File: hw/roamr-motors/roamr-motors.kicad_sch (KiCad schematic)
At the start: 0 parts

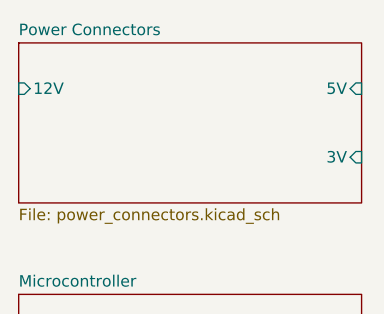
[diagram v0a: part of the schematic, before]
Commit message: Add USB-UART, USB receptacles, ESP32-S3-WROOM-1, switches. TODO: 5V_3V3 LDO, BLDC drivers, encoder SPI, connectors
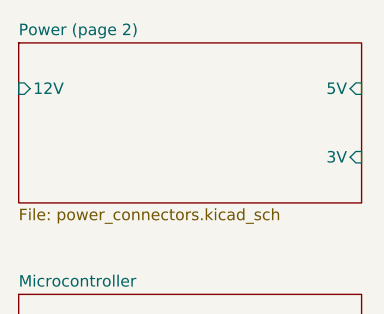
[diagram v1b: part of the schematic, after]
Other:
- sheet Power Connectors renamed Power (page 2)
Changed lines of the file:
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@@
 			(color 0 0 0 0.0000)
 		)
-		(property "Sheetname" "Power Connectors"
+		(property "Sheetname" "Power (page 2)"
 			(at 120.65 43.7384 0)
 			(effects

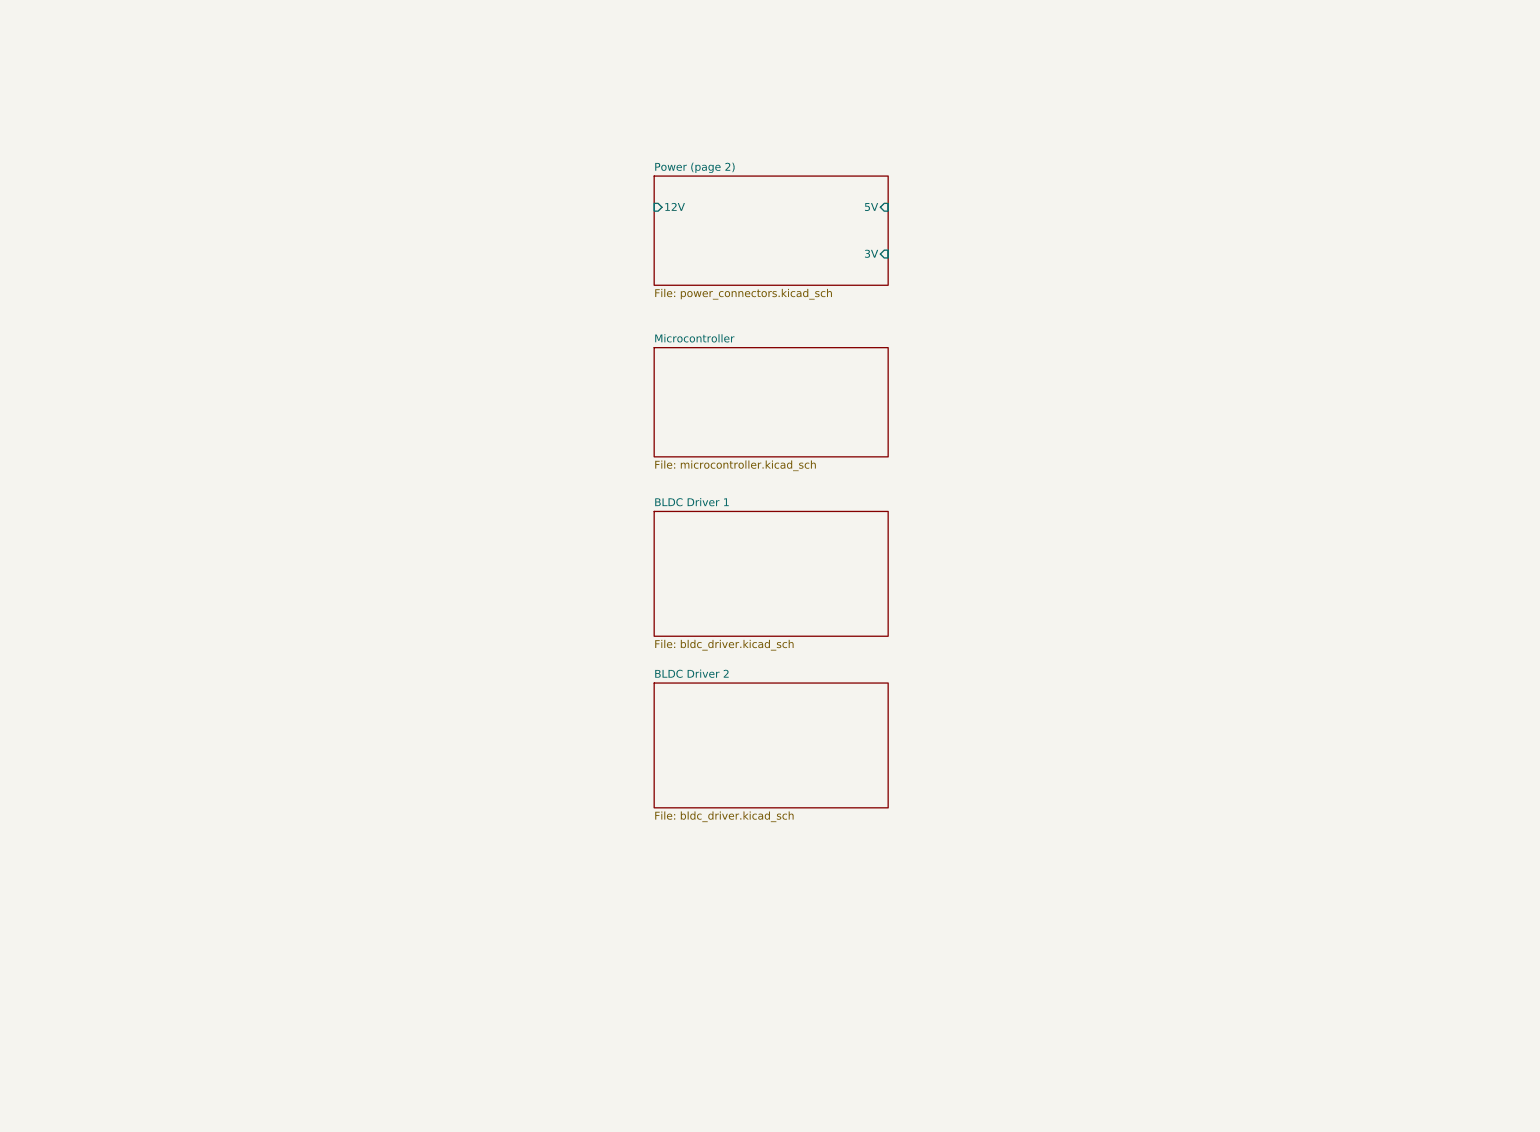
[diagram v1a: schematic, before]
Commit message: just moving around the usb connectors
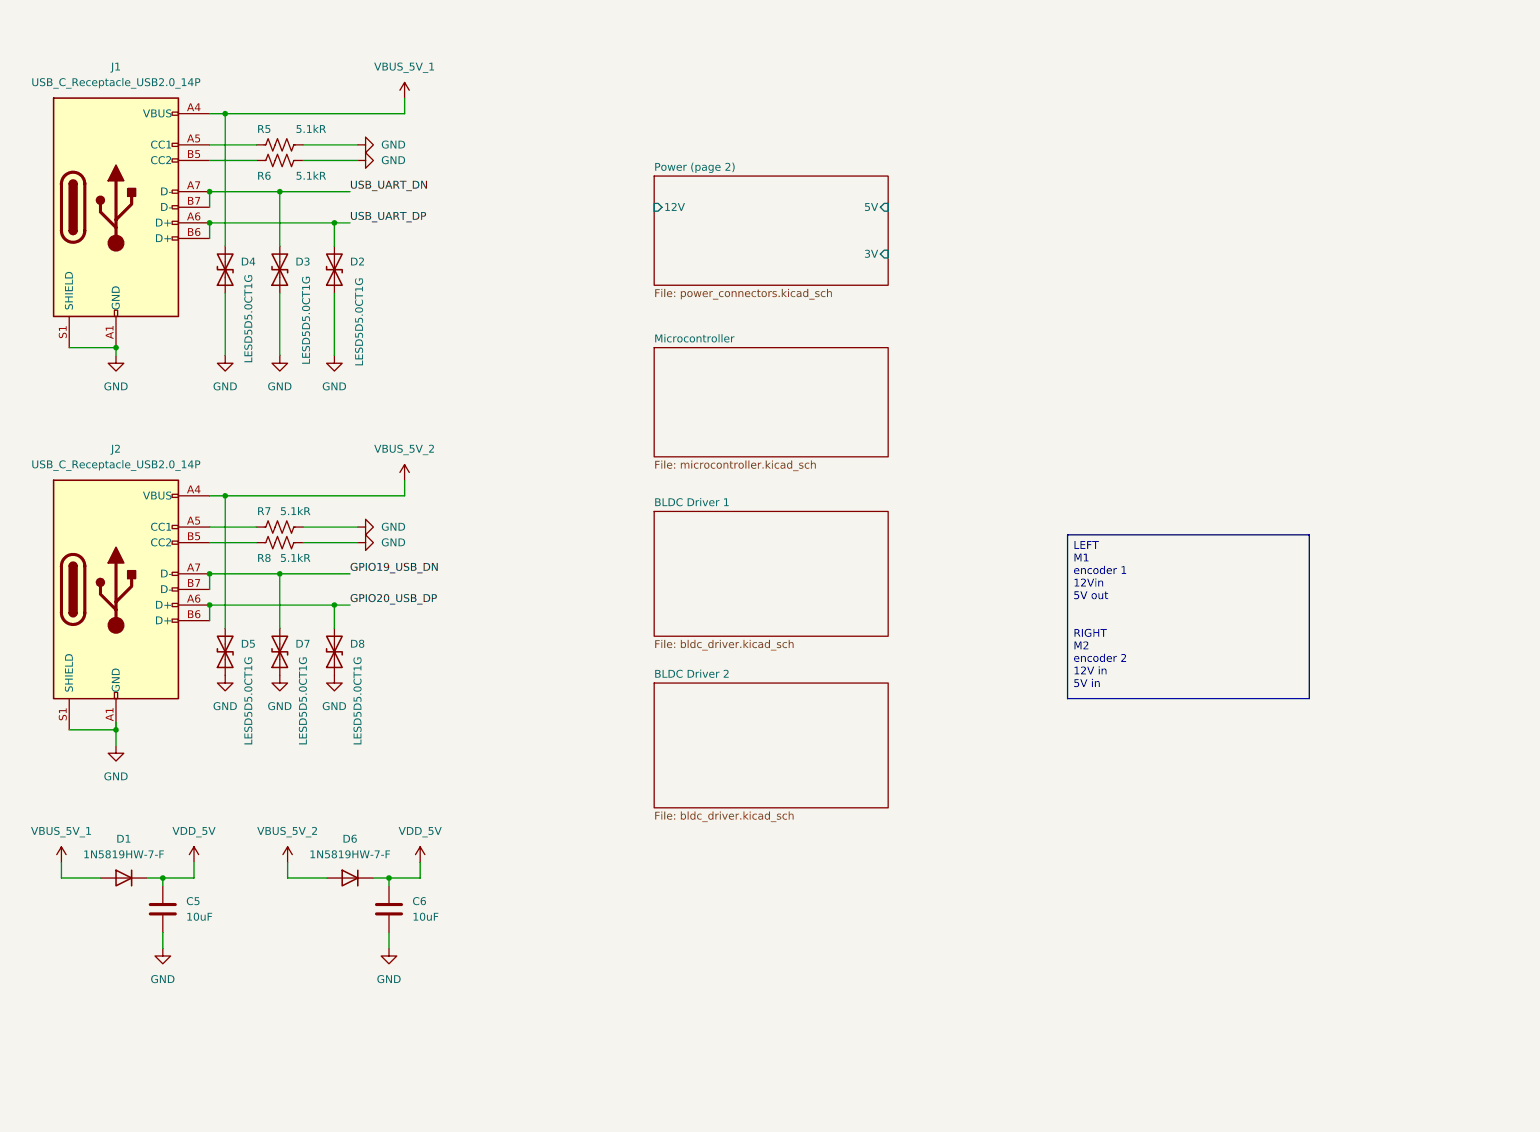
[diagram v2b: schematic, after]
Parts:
- added C5, C6: 10uF, symbol Device:C
- added D1, D6: 1N5819HW-7-F, symbol Device:D
- added D2, D3, D4, D5, D7, D8: LESD5D5.0CT1G, symbol Device:D_TVS
- added J1, J2: USB_C_Receptacle_USB2.0_14P, symbol Connector:USB_C_Receptacle_USB2.0_14P
- added R5, R6, R7, R8: 5.1kR, symbol Device:R_US
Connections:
- new net: J1.A5 (CC1), R5.1
- new net: J2.B5 (CC2), R8.1
- new net: J2.A5 (CC1), R7.1
- new net: J1.B5 (CC2), R6.1
- new net GND: C5.2, C6.2, D2.1 (A1), D3.1 (A1), D4.1 (A1), D5.1 (A1), D7.1 (A1), D8.1 (A1), J1.A1 (GND), J1.A12 (GND), J1.B1 (GND), J1.B12 (GND), J1.S1 (SHIELD), J2.A1 (GND), J2.A12 (GND), J2.B1 (GND), J2.B12 (GND), J2.S1 (SHIELD), R5.2, R6.2, R7.2, R8.2
- new net GPIO19_USB_DN: D7.2 (A2), J2.A7 (D-), J2.B7 (D-)
- new net GPIO20_USB_DP: D8.2 (A2), J2.A6 (D+), J2.B6 (D+)
- new net USB_UART_DN: D3.2 (A2), J1.A7 (D-), J1.B7 (D-)
- new net USB_UART_DP: D2.2 (A2), J1.A6 (D+), J1.B6 (D+)
- new net VBUS_5V_1: D1.2 (A), D4.2 (A2), J1.A4 (VBUS), J1.A9 (VBUS), J1.B4 (VBUS), J1.B9 (VBUS)
- new net VBUS_5V_2: D5.2 (A2), D6.2 (A), J2.A4 (VBUS), J2.A9 (VBUS), J2.B4 (VBUS), J2.B9 (VBUS)
- new net VDD_5V: C5.1, C6.1, D1.1 (K), D6.1 (K)

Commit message: finished schematic and assigning most footprints
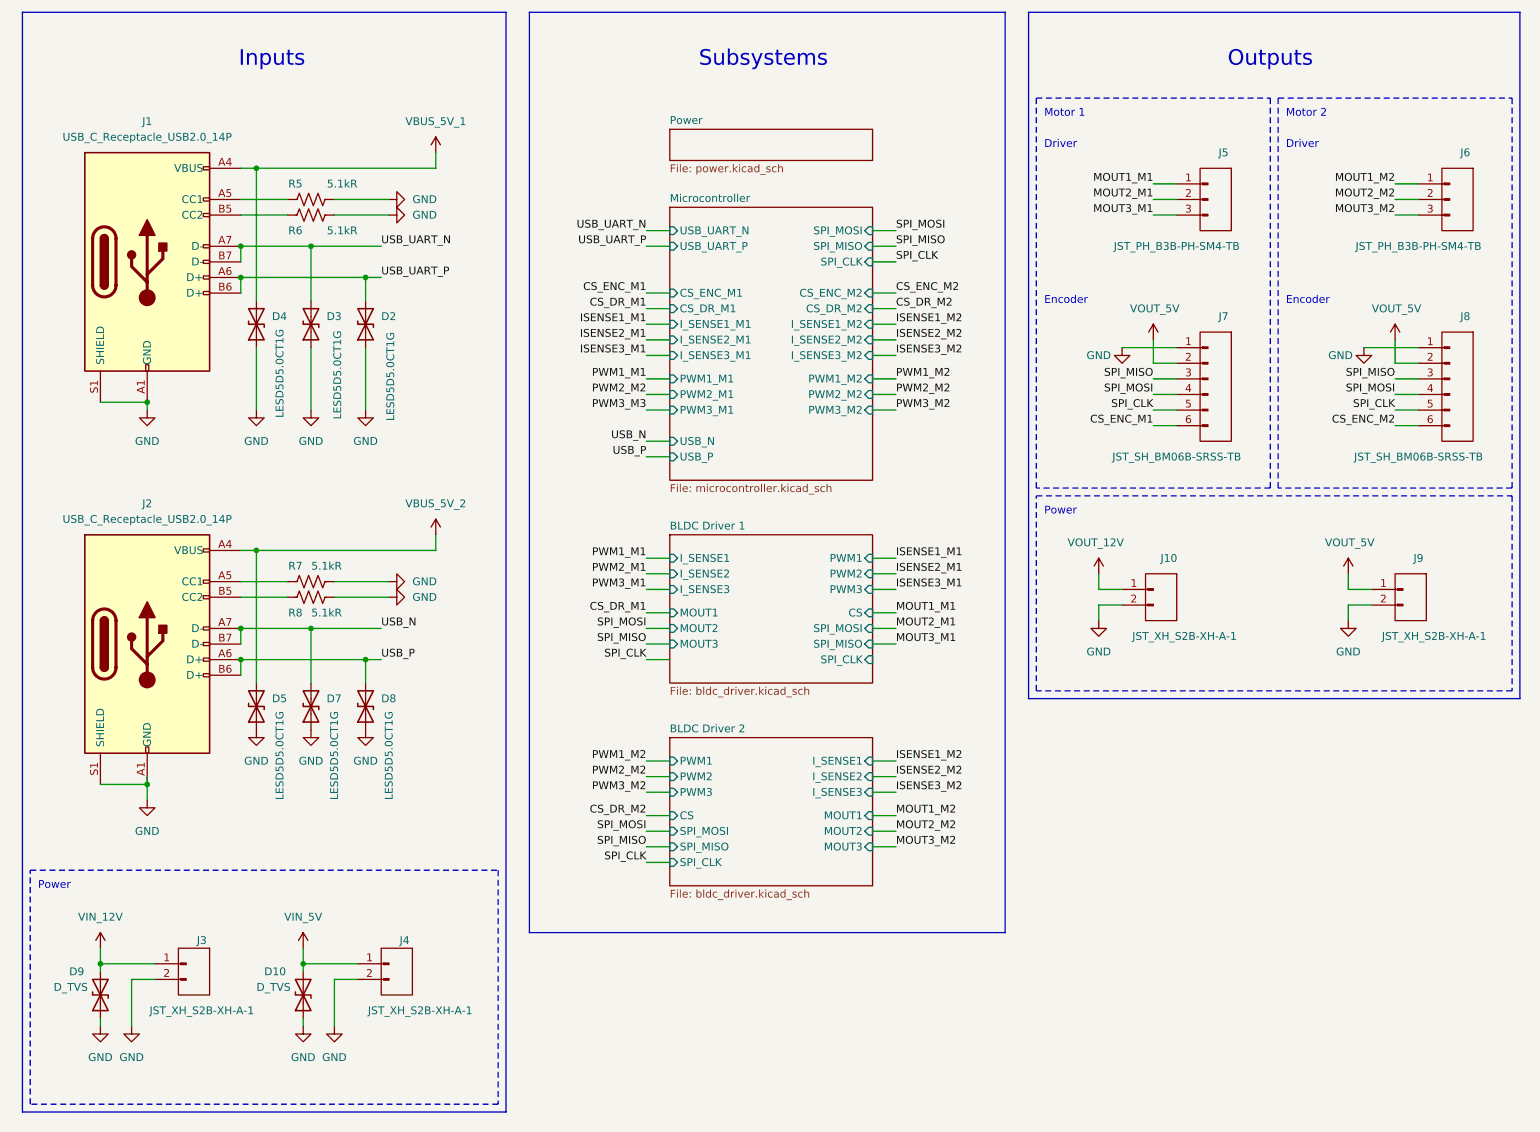
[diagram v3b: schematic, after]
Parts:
- removed C5, C6: 10uF, symbol Device:C
- removed D1, D6: 1N5819HW-7-F, symbol Device:D
- added D10, D9: D_TVS, SMLJ12A-R:DIOM7959X262N, symbol Device:D_TVS
- added J10, J3, J4, J9: JST_XH_S2B-XH-A-1, Connector_JST:JST_XH_S2B-XH-A-1_1x02_P2.50mm_Horizontal, symbol Connector:Conn_01x02_Pin
- added J5, J6: JST_PH_B3B-PH-SM4-TB, Connector_JST:JST_PH_B3B-PH-SM4-TB_1x03-1MP_P2.00mm_Vertical, symbol Connector:Conn_01x03_Pin
- added J7, J8: JST_SH_BM06B-SRSS-TB, Connector_JST:JST_SH_BM06B-SRSS-TB_1x06-1MP_P1.00mm_Vertical, symbol Connector:Conn_01x06_Pin
- J1, J2: footprint (none) -> USB4215_03_A:CONN_8p94X6p5X3p16_12L_GCC
- R5, R6, R7, R8: footprint (none) -> Resistor_SMD:R_0603_1608Metric
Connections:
- net GND: now also D10.1 (A1), D9.1 (A1), J10.2 (Pin_2), J3.2 (Pin_2), J4.2 (Pin_2), J7.1 (Pin_1), J8.1 (Pin_1), J9.2 (Pin_2)
- net GPIO19_USB_DN renamed USB_N
- net GPIO20_USB_DP renamed USB_P
- net USB_UART_DN renamed USB_UART_N
- net USB_UART_DP renamed USB_UART_P
- new net CS_ENC_M1: J7.6 (Pin_6)
- new net CS_ENC_M2: J8.6 (Pin_6)
- new net MOUT1_M1: J5.1 (Pin_1)
- new net MOUT1_M2: J6.1 (Pin_1)
- new net MOUT2_M1: J5.2 (Pin_2)
- new net MOUT2_M2: J6.2 (Pin_2)
- new net MOUT3_M1: J5.3 (Pin_3)
- new net MOUT3_M2: J6.3 (Pin_3)
- new net SPI_CLK: J7.5 (Pin_5), J8.5 (Pin_5)
- new net SPI_MISO: J7.3 (Pin_3), J8.3 (Pin_3)
- new net SPI_MOSI: J7.4 (Pin_4), J8.4 (Pin_4)
- new net VIN_12V: D9.2 (A2), J3.1 (Pin_1)
- new net VIN_5V: D10.2 (A2), J4.1 (Pin_1)
- new net VOUT_12V: J10.1 (Pin_1)
- new net VOUT_5V: J7.2 (Pin_2), J8.2 (Pin_2), J9.1 (Pin_1)
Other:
- removed sheet Power (page 2)
- added sheet Power (power.kicad_sch)
- sheet BLDC Driver 1 ports: added CS, I_SENSE1, I_SENSE2, I_SENSE3, MOUT1, MOUT2, MOUT3, PWM1, PWM2, PWM3, SPI_CLK, SPI_MISO, SPI_MOSI; removed none
- sheet BLDC Driver 2 ports: added CS, I_SENSE1, I_SENSE2, I_SENSE3, MOUT1, MOUT2, MOUT3, PWM1, PWM2, PWM3, SPI_CLK, SPI_MISO, SPI_MOSI; removed none
- sheet Microcontroller ports: added CS_DR_M1, CS_DR_M2, CS_ENC_M1, CS_ENC_M2, I_SENSE1_M1, I_SENSE1_M2, I_SENSE2_M1, I_SENSE2_M2, I_SENSE3_M1, I_SENSE3_M2, PWM1_M1, PWM1_M2, PWM2_M1, PWM2_M2, PWM3_M1, PWM3_M2, SPI_CLK, SPI_MISO, SPI_MOSI, USB_N, USB_P, USB_UART_N, USB_UART_P; removed none
- note added: "Driver"
- note added: "Encoder"
- note added: "Inputs"
- note added: "Motor 1"
- note added: "Motor 2"
- note added: "Outputs"
- note added: "Power"
- note added: "Subsystems"
- company: (none) -> Mechatronics FYDP Group 16
- moved on the sheet: D2, D3, D4, D5, D7, D8, J1, J2, R5, R6, R7, R8

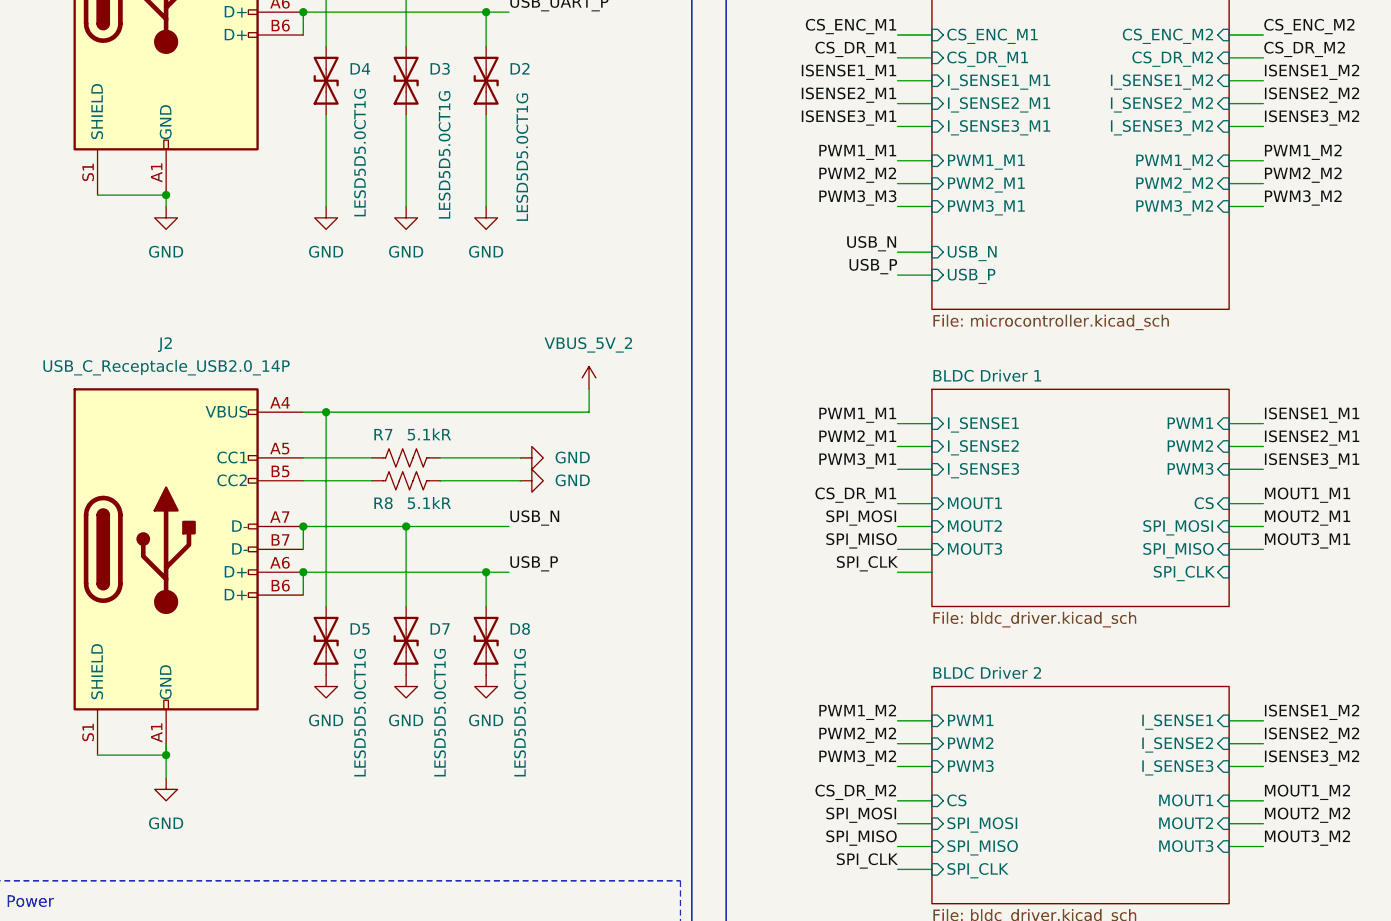
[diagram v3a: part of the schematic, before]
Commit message: added all footprints, starting layout properly
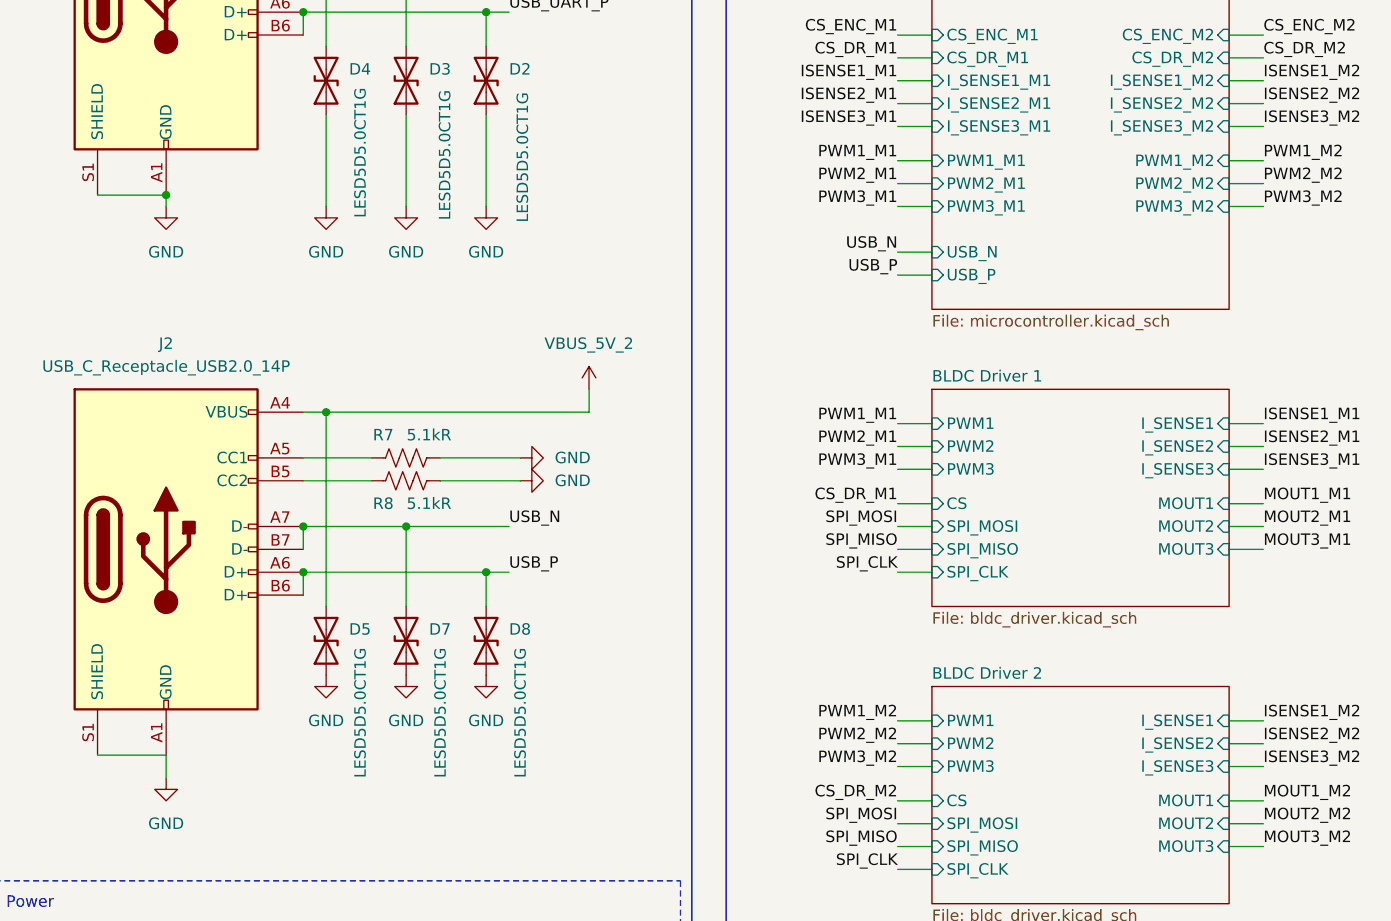
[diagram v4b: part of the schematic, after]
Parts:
- D2, D3, D4, D5, D7, D8: footprint (none) -> LESD5D5.0CT1G:LESD5D50CT1G

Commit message: some more layout
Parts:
- removed J1, J2: USB_C_Receptacle_USB2.0_14P, USB4215_03_A:CONN_8p94X6p5X3p16_12L_GCC, symbol Connector:USB_C_Receptacle_USB2.0_14P
- added J1, J2: USB4215-03-A, CONN_8p94X6p5X3p16_12L_GCC, symbol USB4215_03_A:USB4215-03-A
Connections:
- net GND: now also J1.A1/B12 (GND), J1.B1/A12 (GND), J2.A1/B12 (GND), J2.B1/A12 (GND)
- net USB_N: now also J2.A7 (DN1), J2.B7 (DN2)
- net USB_P: now also J2.A6 (DP1), J2.B6 (DP2)
- net USB_UART_N: now also J1.A7 (DN1), J1.B7 (DN2)
- net USB_UART_P: now also J1.A6 (DP1), J1.B6 (DP2)
- net VBUS_5V_1: now also J1.A4/B9 (VBUS), J1.B4/A9 (VBUS)
- net VBUS_5V_2: now also J2.A4/B9 (VBUS), J2.B4/A9 (VBUS)
- net at R5.1: now also J1.A5 (CC1)
- net at R8.1: now also J2.B5 (CC2)
- net at R7.1: now also J2.A5 (CC1)
- net at R6.1: now also J1.B5 (CC2)
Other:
- moved on the sheet: D10, D2, D3, D4, D5, D7, D8, D9, J3, J4, R5, R6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

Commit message: more layout, i think i get do it on one side
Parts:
- D1: renamed from D9; value D_TVS -> SMLJ12A-R
- D4: renamed from D10; value D_TVS -> SMLJ12A-R
- J2: renamed from J1; footprint CONN_8p94X6p5X3p16_12L_GCC -> USB4215_03_A:CONN_8p94X6p5X3p16_12L_GCC
- J3: renamed from J2; footprint CONN_8p94X6p5X3p16_12L_GCC -> USB4215_03_A:CONN_8p94X6p5X3p16_12L_GCC
- renumbered D4 to D2, D5 to D3, D3 to D5, D7 to D6, D2 to D7, J3 to J1, J8 to J10, J10 to J5, J5 to J6, J9 to J8, J6 to J9, R5 to R1, R6 to R2, R7 to R3, R8 to R4
